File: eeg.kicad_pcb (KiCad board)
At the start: 2 copper layers, 75.7 x 54.9 mm, 128 parts, among them J1 USB_B_Mini, J2 Conn_01x10_MountingPin, U1 STM32F446RE, U10 -.+2.5V.+3.3V-GND, U11 +5V, U12 RN4678-V_RM100, U2 ADS1299-8CHANNEL, U3 LD39050PU33R, U4 TPS60403DBVT, U5 TPS73225DBVT, U6 TPS72325DBVT, U61 Electrode1, U7 DATA, U8 Electrode2, U9 ADC_REFGND_GPIO, Y1 16.00Mhz

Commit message: Update .gitignore
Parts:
- removed U61: Electrode1, ADS1299IPAG:openldhardware
- removed U8: Electrode2, ADS1299IPAG:openldhardware
- added C1001: 1uF, Capacitor_SMD:C_0603_1608Metric, F.Cu at (30.7, 20.1)
- added D1: LED, LED_SMD:LED_0603_1608Metric, F.Cu at (74.2, 55.9)
- added J3: Conn_02x20_Counter_Clockwise, Connector_PinHeader_1.27mm:PinHeader_2x20_P1.27mm_Vertical, F.Cu at (39.8, 58.9)
- added J4: Conn_02x20_Counter_Clockwise, Connector_PinHeader_1.27mm:PinHeader_2x20_P1.27mm_Vertical, F.Cu at (39.8, 31.8)
- added R20: R_Small, Resistor_SMD:R_0603_1608Metric, F.Cu at (101.6, 61.4)
- added R21: R_Small, Resistor_SMD:R_0603_1608Metric, F.Cu at (105.6, 61.4)
- added R22: R_Small, Resistor_SMD:R_0603_1608Metric, F.Cu at (109.6, 61.4)
- moved HC7361 28.6 mm to (76.8, 70.3)
- moved C101 26.5 mm to (86.7, 42.8)
- moved C100 26.5 mm to (85.3, 43.3)
- moved U3 25.9 mm to (88.9, 44.0)
- moved C103 25.5 mm to (93.0, 43.0)
- moved C102 25.4 mm to (91.5, 43.4)
- moved D2 23.9 mm to (101.3, 58.0)
- moved D3 23.7 mm to (105.6, 58.5)
- moved D4 23.7 mm to (109.6, 58.5)
- moved C59 15.5 mm to (94.9, 39.7)
- moved C110 12.6 mm to (74.9, 37.6)
- moved U4 12.6 mm to (65.6, 37.6)
- moved C105 12.6 mm to (60.8, 37.6)
- moved C106 12.6 mm to (62.3, 37.6)
- moved L1 12.6 mm to (59.1, 37.6)
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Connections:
- C100 pad 2: GNDA -> GNDD
- C101 pad 2: GNDA -> GNDD
- C102 pad 2: GNDA -> GNDD
- C103 pad 2: GNDA -> GNDD
- C42 pad 1: GND -> GNDD
- C56 pad 1: GNDREF -> GNDD
- C59 pad 1: GNDREF -> GNDD
- C61 pad 2: GNDREF -> GNDD
- C64 pad 1: GNDREF -> GNDD
- C67 pad 2: GNDREF -> GNDD
- C71 pad 2: GNDREF -> GNDD
- C72 pad 2: GNDREF -> GNDD
- C73 pad 2: GNDREF -> GNDD
- C74 pad 2: GNDREF -> GNDD
- C75 pad 1: GNDREF -> GNDD
- C76 pad 2: GNDREF -> GNDD
- C79 pad 2: GNDREF -> GNDD
- C80 pad 2: GND -> GNDD
- C81 pad 2: GND -> GNDD
- C83 pad 2: GND -> GNDD
- R26 pad 1: GND -> GNDD
- S3 pad 1: GND -> GNDD
- S3 pad 2: GND -> GNDD
- S3 pad 3: (no net) -> Net-(C83-Pad1)
- U1 pad 18: GNDREF -> GNDD
- U1 pad 31: GNDREF -> GNDD
- U1 pad 47: GNDREF -> GNDD
- U3 pad 2: GNDA -> GNDD
- U3 pad 7: GNDA -> GNDD
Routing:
- net +5V: track 18.2 -> 75.2 mm, vias 0 -> 5
- net +2V5: track 12.2 -> 61.9 mm
- net /BIASINV: track 0.00 -> 30.5 mm
- net -2V5: track 0.04 -> 30.1 mm, vias 0 -> 3
- net -5V: track 1.82 -> 27.5 mm, vias 0 -> 3
- net /BIASIN: track 2.96 -> 28.0 mm
- net SCLK: track 0.00 -> 19.0 mm
- net PWDN: track 0.00 -> 18.3 mm
- net RESET: track 0.00 -> 17.8 mm
- net START: track 0.00 -> 16.3 mm
- net GNDA: track 143.3 -> 159.3 mm, vias 34 -> 31
- net Net-(C105-Pad1): track 18.4 -> 34.3 mm, vias 0 -> 2
- net /CLK: track 0.00 -> 14.3 mm, vias 0 -> 2
- net +3V3: track 14.7 -> 1.27 mm, vias 1 -> 0
- net Net-(C118-Pad1): track 0.00 -> 10.9 mm
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- removed copper zone on B.Cu, net GNDA

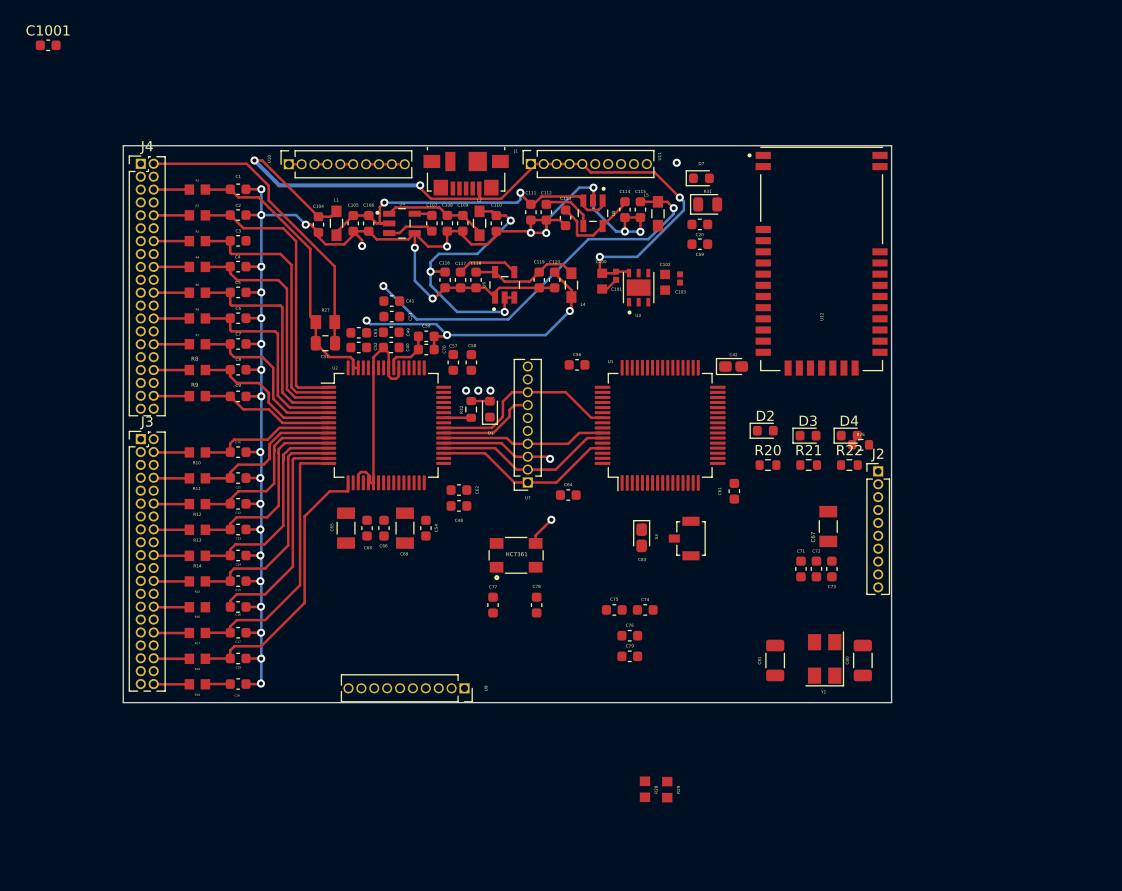
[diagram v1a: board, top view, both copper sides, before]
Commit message: EVQ Tactile Button footprint changed
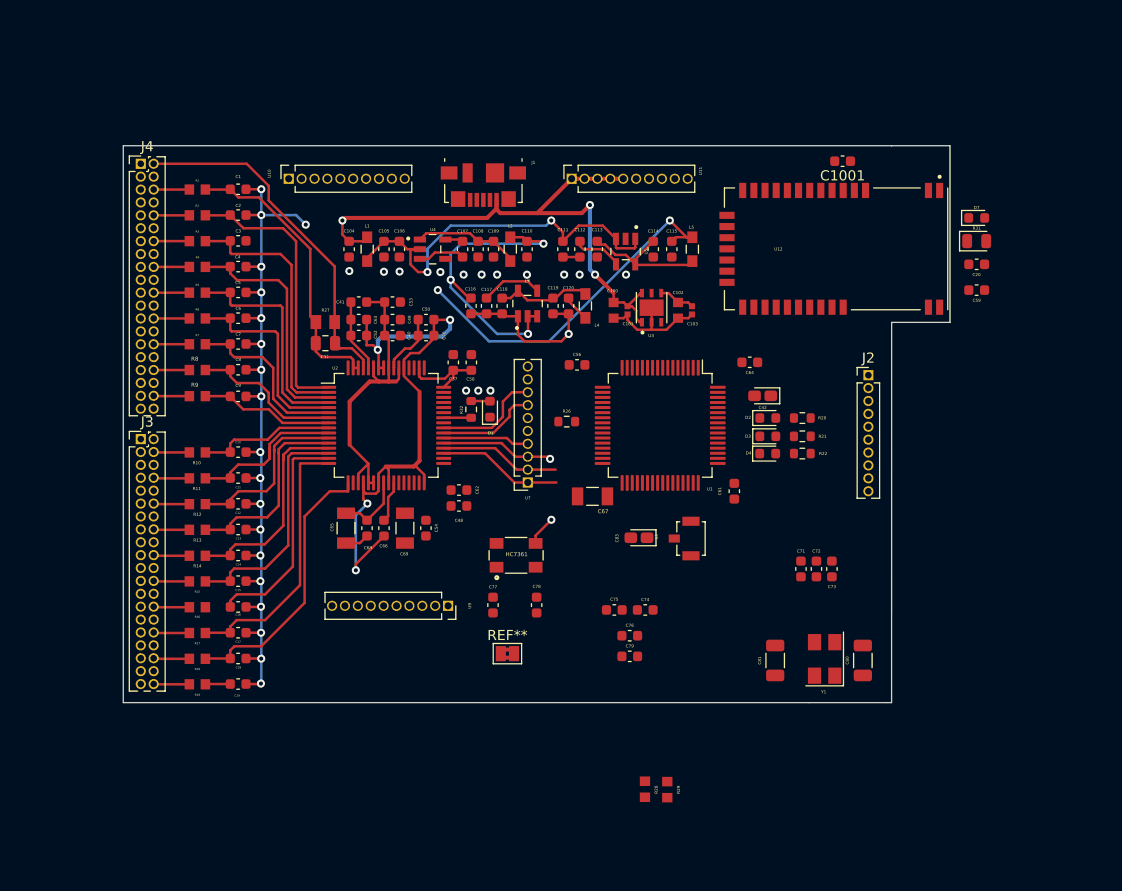
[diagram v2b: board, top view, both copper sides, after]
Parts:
- added REF**: SolderJumper-2_P1.3mm_Bridged2Bar_Pad1.0x1.5mm, Jumper:SolderJumper-2_P1.3mm_Bridged2Bar_Pad1.0x1.5mm, F.Cu at (75.9, 80.0)
- moved C1001 79.1 mm to (109.0, 31.5), turned to 180 degrees
- moved R26 29.0 mm to (81.8, 57.1)
- moved C59 27.6 mm to (122.2, 44.2)
- moved C20 27.6 mm to (122.2, 41.7)
- moved D7 27.4 mm to (122.2, 37.1)
- moved R31 26.7 mm to (122.2, 39.4)
- moved C67 23.4 mm to (84.3, 64.5), turned to 180 degrees
- moved C64 22.2 mm to (99.8, 51.3), turned to 180 degrees
- moved J2 9.52 mm to (111.5, 52.6)
- moved U9 8.29 mm to (70.1, 75.3)
- moved D4 8.22 mm to (101.6, 60.3)
- moved R20 5.74 mm to (105.0, 56.8)
- moved C115 4.97 mm to (92.1, 40.2)
- moved U5 4.96 mm to (87.6, 40.4)
- moved C112 4.92 mm to (83.1, 40.2)
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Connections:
- C1001 pad 1: GNDREF -> GNDD
- C65 pad 2: /-2.5V -> -2V5
- C68 pad 1: /-2.5V -> -2V5
- J1 pad 5: GNDREF -> GNDD
- J1 pad 6: GNDREF -> GNDD
- U10 pad 10: GND -> GNDD
- U10 pad 7: GND -> GNDD
- U10 pad 8: GND -> GNDD
- U10 pad 9: GND -> GNDD
- U11 pad 10: GND -> GNDD
- U11 pad 6: GND -> GNDD
- U11 pad 7: GND -> GNDD
- U11 pad 8: GND -> GNDD
- U11 pad 9: GND -> GNDD
- U12 pad 1: GNDREF -> GNDD
- U12 pad 2: GNDREF -> GNDD
- U12 pad 3: GNDREF -> GNDD
- U12 pad 31: GNDREF -> GNDD
- U12 pad 32: GNDREF -> GNDD
- U12 pad 33: GNDREF -> GNDD
- U2 pad 25: /-2.5V -> -2V5
- U2 pad 31: GNDREF -> /GNDREF
- U2 pad 33: GNDREF -> /GNDREF
- U2 pad 49: GNDREF -> /GNDREF
- U2 pad 51: GNDREF -> /GNDREF
- U7 pad 10: GND -> GNDA
- U7 pad 9: GND -> GNDA
- U9 pad 6: GNDREF -> GNDD
- U9 pad 7: GNDREF -> GNDD
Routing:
- net GNDA: track 159.3 -> 104.7 mm, vias 31 -> 34
- net -2V5: track 30.1 -> 64.9 mm, vias 3 -> 4
- net +5V: track 75.2 -> 57.9 mm, vias 5 -> 3
- net +3V3: track 1.27 -> 12.1 mm
- net GNDD: track 1.75 -> 11.6 mm
- net SCLK: track 19.0 -> 10.6 mm
- net START: track 16.3 -> 8.52 mm
- net /VREFP: track 0.00 -> 6.72 mm
- net PWDN: track 18.3 -> 12.3 mm
- net RESET: track 17.8 -> 11.9 mm
- net Net-(C105-Pad1): track 34.3 -> 39.1 mm
- net Net-(C113-Pad1): track 9.15 -> 13.6 mm
- net /BIASINV: track 30.5 -> 34.8 mm
- net Net-(C66-Pad1): track 0.00 -> 4.09 mm
- net -5V: track 27.5 -> 31.4 mm
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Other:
- board size 75.7 x 54.9 mm -> 81.4 x 54.9 mm

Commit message: Via sizes changed 04mm to 1.2mm and bugs fixed
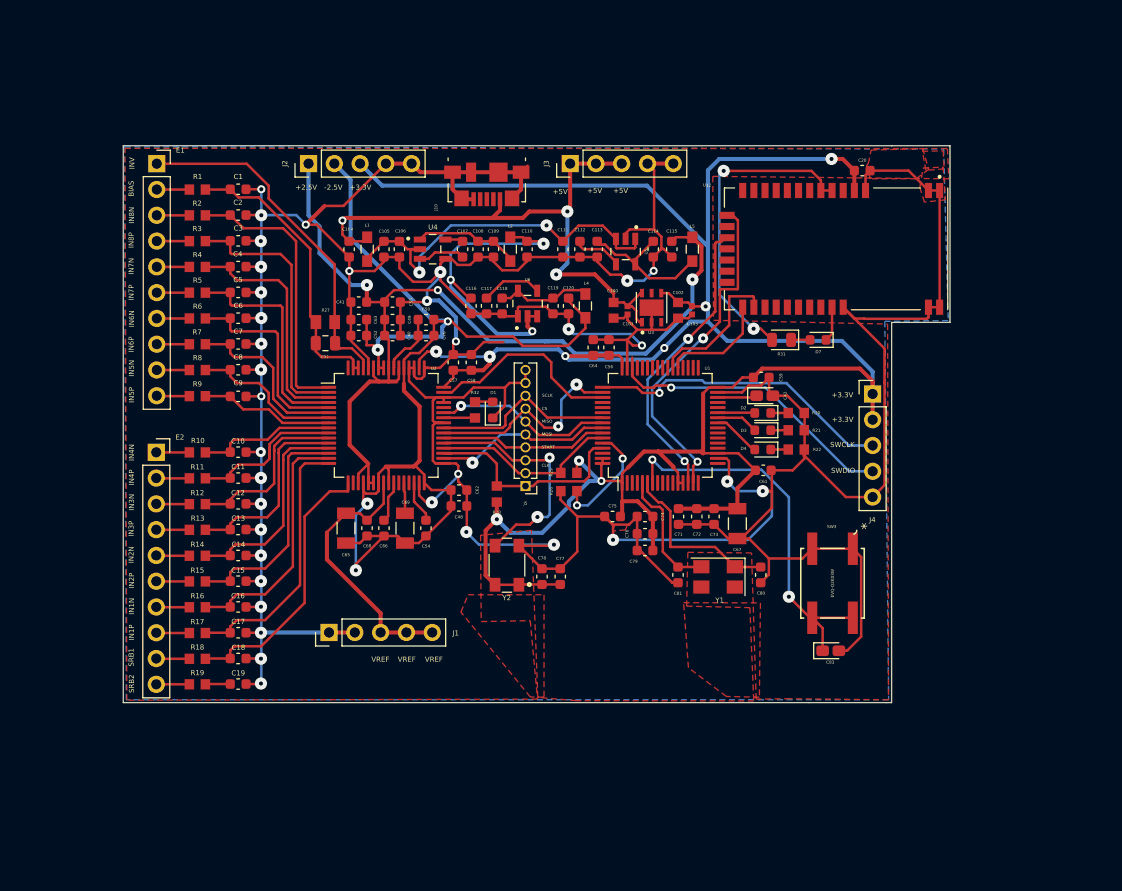
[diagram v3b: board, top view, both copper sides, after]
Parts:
- removed C1001: 1uF, Capacitor_SMD:C_0603_1608Metric
- removed HC7361: 2.048mhz, ERA-3A:OSCCC500X320X150N
- removed REF**: SolderJumper-2_P1.3mm_Bridged2Bar_Pad1.0x1.5mm, Jumper:SolderJumper-2_P1.3mm_Bridged2Bar_Pad1.0x1.5mm
- removed S3: SW_MEC_5G, Button_Switch_SMD:SW_SPST_B3U-1100P
- removed U10: -.+2.5V.+3.3V-GND, Connector_PinSocket_1.27mm:PinSocket_1x10_P1.27mm_Vertical
- removed U11: +5V, Connector_PinSocket_1.27mm:PinSocket_1x10_P1.27mm_Vertical
- removed U7: DATA, Connector_PinSocket_1.27mm:PinSocket_1x10_P1.27mm_Vertical
- removed U9: ADC_REFGND_GPIO, Connector_PinSocket_1.27mm:PinSocket_1x10_P1.27mm_Vertical
- added E1: Conn_01x10_Male, Connector_PinSocket_2.54mm:PinSocket_1x10_P2.54mm_Vertical, F.Cu at (41.4, 31.7)
- added E2: Conn_01x10_Male, Connector_PinSocket_2.54mm:PinSocket_1x10_P2.54mm_Vertical, F.Cu at (41.4, 60.2)
- added J1: Conn_01x05_Male, Connector_PinHeader_2.54mm:PinHeader_1x05_P2.54mm_Vertical, F.Cu at (58.4, 77.9)
- added J5: Conn_01x10, Connector_PinHeader_1.27mm:PinHeader_1x10_P1.27mm_Vertical, F.Cu at (77.7, 63.5)
- added SW3: EVQ-Q2K03W, footprints:EVQ-Q2K03W, F.Cu at (108.0, 73.1)
- added Y2: 2.048mhz, ERA-3A:OSCCC500X320X150N, F.Cu at (75.9, 71.3)
- C80, C81: footprint Capacitor_SMD:C_1206_3216Metric -> Capacitor_SMD:C_0603_1608Metric
- J2: value Conn_01x10_MountingPin -> Conn_01x05_Male; footprint Connector_PinHeader_1.27mm:PinHeader_1x10_P1.27mm_Vertical -> Connector_PinHeader_2.54mm:PinHeader_1x05_P2.54mm_Vertical
- J3, J4: value Conn_02x20_Counter_Clockwise -> Conn_01x05_Male; footprint Connector_PinHeader_1.27mm:PinHeader_2x20_P1.27mm_Vertical -> Connector_PinHeader_2.54mm:PinHeader_1x05_P2.54mm_Vertical
- R20, R21, R22, R26, R32: footprint Resistor_SMD:R_0603_1608Metric -> ERA-3A:RESC1608X55N
- moved J4 75.6 mm to (111.9, 54.4)
- moved J2 59.0 mm to (56.4, 31.7), turned to 90 degrees
- moved J3 50.3 mm to (82.1, 31.7), turned to 90 degrees
- moved R29 32.7 mm to (82.0, 62.2), turned to 0 degrees
- moved R28 32.5 mm to (74.9, 64.3)
- moved C59 22.9 mm to (101.0, 52.8)
- moved C83 21.9 mm to (107.8, 79.7), turned to 0 degrees
- moved R31 21.5 mm to (103.0, 49.1), turned to 180 degrees
- moved D7 19.7 mm to (106.5, 49.1), turned to 180 degrees
- moved C64 15.5 mm to (84.4, 49.9), turned to 270 degrees
- moved C20 14.6 mm to (110.9, 32.4), turned to 180 degrees
- moved C67 14.5 mm to (98.6, 67.2), turned to 270 degrees
- moved Y1 13.2 mm to (96.7, 72.5), turned to 180 degrees
- moved C80 13.1 mm to (100.9, 72.2), turned to 270 degrees
- moved C71 13.1 mm to (92.8, 66.5), turned to 270 degrees
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- renumbered J1 to J10
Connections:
- net /LD033_O renamed Net-(R31-Pad2)
- net /NSS renamed Net-(U1-Pad20)
- net /VREFP renamed VREFP
- C100 pad 2: GNDD -> GNDA
- C101 pad 2: GNDD -> GNDA
- C102 pad 2: GNDD -> GNDA
- C103 pad 2: GNDD -> GNDA
- C20 pad 1: Net-(C20-Pad1) -> GNDA
- C42 pad 1: GNDD -> Net-(C42-Pad1)
- C42 pad 2: Net-(C42-Pad2) -> GNDA
- C56 pad 1: GNDD -> GNDA
- C59 pad 1: GNDD -> GNDA
- C61 pad 2: GNDD -> GNDA
- C64 pad 1: GNDD -> GNDA
- C67 pad 2: GNDD -> GNDA
- C71 pad 2: GNDD -> GNDA
- C72 pad 2: GNDD -> GNDA
- C73 pad 2: GNDD -> GNDA
- C74 pad 2: GNDD -> GNDA
- C75 pad 1: GNDD -> GNDA
- C76 pad 2: GNDD -> GNDA
- C79 pad 2: GNDD -> GNDA
- C80 pad 2: GNDD -> GNDA
- C81 pad 2: GNDD -> GNDA
- C83 pad 2: GNDD -> GNDA
- J10 pad 5: GNDD -> GNDA
- J10 pad 6: GNDD -> GNDA
- J2 pad 1: Net-(J2-Pad1) -> +2V5
- J2 pad 2: Net-(J2-Pad2) -> -2V5
- J2 pad 3: Net-(J2-Pad3) -> +3V3
- J2 pad 4: Net-(J2-Pad4) -> GNDA
- J2 pad 5: Net-(J2-Pad5) -> GNDA
- J3 pad 1: /+2.5V -> +5V
- J3 pad 2: /-2.5V -> +5V
- J3 pad 3: /+2.5V -> +5V
- J3 pad 4: /-2.5V -> GNDA
- J3 pad 5: /+2.5V -> GNDA
- J4 pad 1: /+2.5V -> +3V3
- J4 pad 2: /-2.5V -> +3V3
- J4 pad 3: /+2.5V -> SWCLK
- J4 pad 4: /-2.5V -> SWDIO
- J4 pad 5: /+2.5V -> GNDA
- R20 pad 1: GNDD -> Net-(D2-Pad1)
- R20 pad 2: Net-(D2-Pad1) -> GNDA
- R21 pad 1: GNDD -> Net-(D3-Pad1)
- R21 pad 2: Net-(D3-Pad1) -> GNDA
- R22 pad 1: GNDD -> Net-(D4-Pad1)
- R22 pad 2: Net-(D4-Pad1) -> GNDA
- R26 pad 1: GNDD -> GNDA
- U1 pad 18: GNDD -> GNDA
- U1 pad 25: Net-(U1-Pad25) -> Net-(D4-Pad2)
- U1 pad 26: Net-(U1-Pad26) -> Net-(D3-Pad2)
- U1 pad 27: Net-(U1-Pad27) -> Net-(D2-Pad2)
- U1 pad 30: Net-(C42-Pad2) -> Net-(C42-Pad1)
- U1 pad 31: GNDD -> GNDA
- U1 pad 40: Net-(D4-Pad2) -> Net-(U1-Pad40)
- U1 pad 41: Net-(D3-Pad2) -> Net-(U1-Pad41)
- U1 pad 42: Net-(D2-Pad2) -> Net-(U1-Pad42)
- U1 pad 47: GNDD -> GNDA
- U1 pad 50: Net-(U1-Pad50) -> CS
- U1 pad 51: Net-(U1-Pad51) -> DRDY
- U12 pad 1: GNDD -> GNDA
- U12 pad 2: GNDD -> GNDA
- U12 pad 3: GNDD -> GNDA
- U12 pad 31: GNDD -> GNDA
- U12 pad 32: GNDD -> GNDA
- U12 pad 33: GNDD -> GNDA
- U12 pad 4: Net-(C20-Pad1) -> +3V3
- U2 pad 31: /GNDREF -> GNDA
- U2 pad 33: /GNDREF -> GNDA
- U2 pad 34: Net-(U2-Pad34) -> MOSI
- U2 pad 43: Net-(U2-Pad43) -> MISO
- U2 pad 47: Net-(U2-Pad47) -> DRDY
- U2 pad 49: /GNDREF -> GNDA
- U2 pad 51: /GNDREF -> GNDA
- U3 pad 2: GNDD -> GNDA
- U3 pad 7: GNDD -> GNDA
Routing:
- net GNDA: track 104.7 -> 514.1 mm, vias 34 -> 35
- net +3V3: track 12.1 -> 248.4 mm, vias 0 -> 9
- net -2V5: track 64.9 -> 116.7 mm
- net Net-(C83-Pad1): track 0.00 -> 38.1 mm, vias 0 -> 2
- net /RN46CTS: track 0.00 -> 34.6 mm, vias 0 -> 2
- net Net-(R31-Pad2): track 0.00 -> 31.5 mm, vias 0 -> 2
- net SWCLK: track 0.00 -> 30.3 mm, vias 0 -> 1
- net SWDIO: track 0.00 -> 29.6 mm, vias 0 -> 1
- net /RN46RTS: track 0.00 -> 29.4 mm, vias 0 -> 2
- net +2V5: track 64.7 -> 93.0 mm, vias 2 -> 3
- net VREFP: track 6.72 -> 27.3 mm
- net DRDY: track 0.00 -> 19.8 mm
- net MOSI: track 0.00 -> 17.7 mm, vias 0 -> 1
- net MISO: track 0.00 -> 17.6 mm, vias 0 -> 1
- net Net-(C80-Pad1): track 0.00 -> 17.1 mm
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- added copper zone on B.Cu, net GNDA
- added copper zone on F.Cu, net GNDA
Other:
- board text added: "+2.5V"
- board text added: "+3.3V"
- board text added: "+5V"
- board text added: "-2.5V"
- board text added: "BIAS"
- board text added: "CLK"
- board text added: "CS"
- board text added: "IN1N"
- board text added: "IN1P"
- board text added: "IN2N"
- board text added: "IN2P"
- board text added: "IN3N"
- board text added: "IN3P"
- board text added: "IN4N"
- board text added: "IN4P"
- board text added: "IN5N"
- board text added: "IN5P"
- board text added: "IN6N"
- board text added: "IN6P"
- board text added: "IN7N"
- board text added: "IN7P"
- board text added: "IN8N"
- board text added: "IN8P"
- board text added: "INV"
- board text added: "MISO"
- board text added: "MOSI"
- board text added: "SCLK"
- board text added: "SRB1"
- board text added: "SRB2"
- board text added: "START"
- board text added: "SWCLK"
- board text added: "SWDIO"
- board text added: "VREF"

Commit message: ground tracks removed
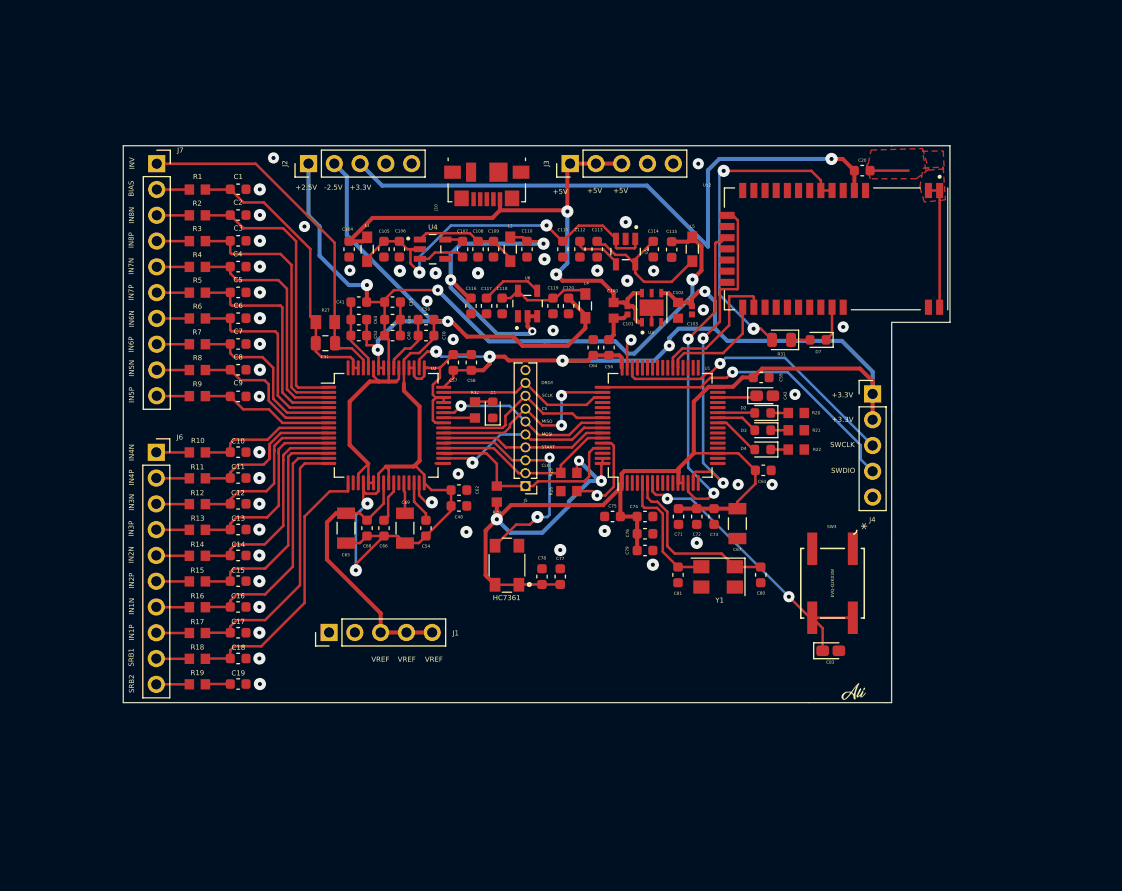
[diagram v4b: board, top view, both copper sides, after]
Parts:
- added G***: LOGO, ali1:ali1, F.Cu at (110.1, 83.7)
- turned C74 to 0 degrees
- turned C76 to 0 degrees
- turned C79 to 0 degrees
- renumbered Y2 to HC7361, E2 to J6, E1 to J7
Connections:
- J4 pad 3: SWCLK -> SWDIO
- J4 pad 4: SWDIO -> SWCLK
- J5 pad 9: GNDA -> DRDY
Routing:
- net GNDA: track 514.1 -> 59.5 mm, vias 35 -> 47
- net Net-(C83-Pad1): track 38.1 -> 29.4 mm
- net +3V3: track 248.4 -> 255.8 mm
- net /RN46RTS: track 29.4 -> 32.0 mm
- net DRDY: track 19.8 -> 17.2 mm
- net SWCLK: track 30.3 -> 32.8 mm
- net +5V: track 59.0 -> 56.8 mm, vias 3 -> 2
- net Net-(R26-Pad2): track 11.3 -> 9.45 mm, vias 2 -> 1
- net +2V5: track 93.0 -> 91.9 mm
- net Net-(C113-Pad1): track 15.3 -> 16.1 mm
- net Net-(C81-Pad1): track 13.4 -> 12.8 mm
- net VREFP: track 27.3 -> 27.8 mm
- net /BIASINV: track 34.4 -> 34.9 mm
- removed copper zone on B.Cu, net GNDA
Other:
- board text added: "DRDY"
